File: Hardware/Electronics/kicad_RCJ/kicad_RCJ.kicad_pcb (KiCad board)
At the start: 2 copper layers, 71 parts, among them J10 Conn_01x04_M1_extra, J11 Conn_01x04_M2_extra, J12 Conn_01x04_M3_extra, J13 Conn_01x04_M4_extra, J14 Conn_01x06_teensy_left_extra, J15 Conn_01x04_teensy_right_extra, J16 Conn_01x07_IO_expander_extra, J17 Conn_02x03_I2C, J18 Conn_02x05_3V3_GND, J19 Conn_02x05_5V_GND, J2 Conn_01x06_IMU_extra, J20 Conn_01x06_BNO085_extra, J21 Conn_01x06_ISM20948_extra, J22 Conn_01x02_LSM5DSOX_LIS3MDL_e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, J3 Conn_01x02_colsens_interrupt, J4 Conn_01x02_5V, J5 Conn_01x02_3V3, J6 Conn_01x02_I2C1, J7 Conn_01x01_LOP, J8 Conn_01x03_IO_expander_interr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, J9 Conn_01x06_LED, M5 Servo1, M6 Servo2, U1 DRV8874, U12 VL53L0/1X, U13 VL53L0/1X, U14 VL53L0/1X, U15 VL53L0/1X, U16 VL53L0/1X, U17 VL53L0/1X, U18 VL53L0/1X, U2 DRV8874, U20 BNO085, U21 ICM20948, U22 LSM6DSOX+LIS3MDL, U23 TCS34725, U24 APDS9960, U25 VL53L0/1X, U3 DRV8874, U4 DRV8874

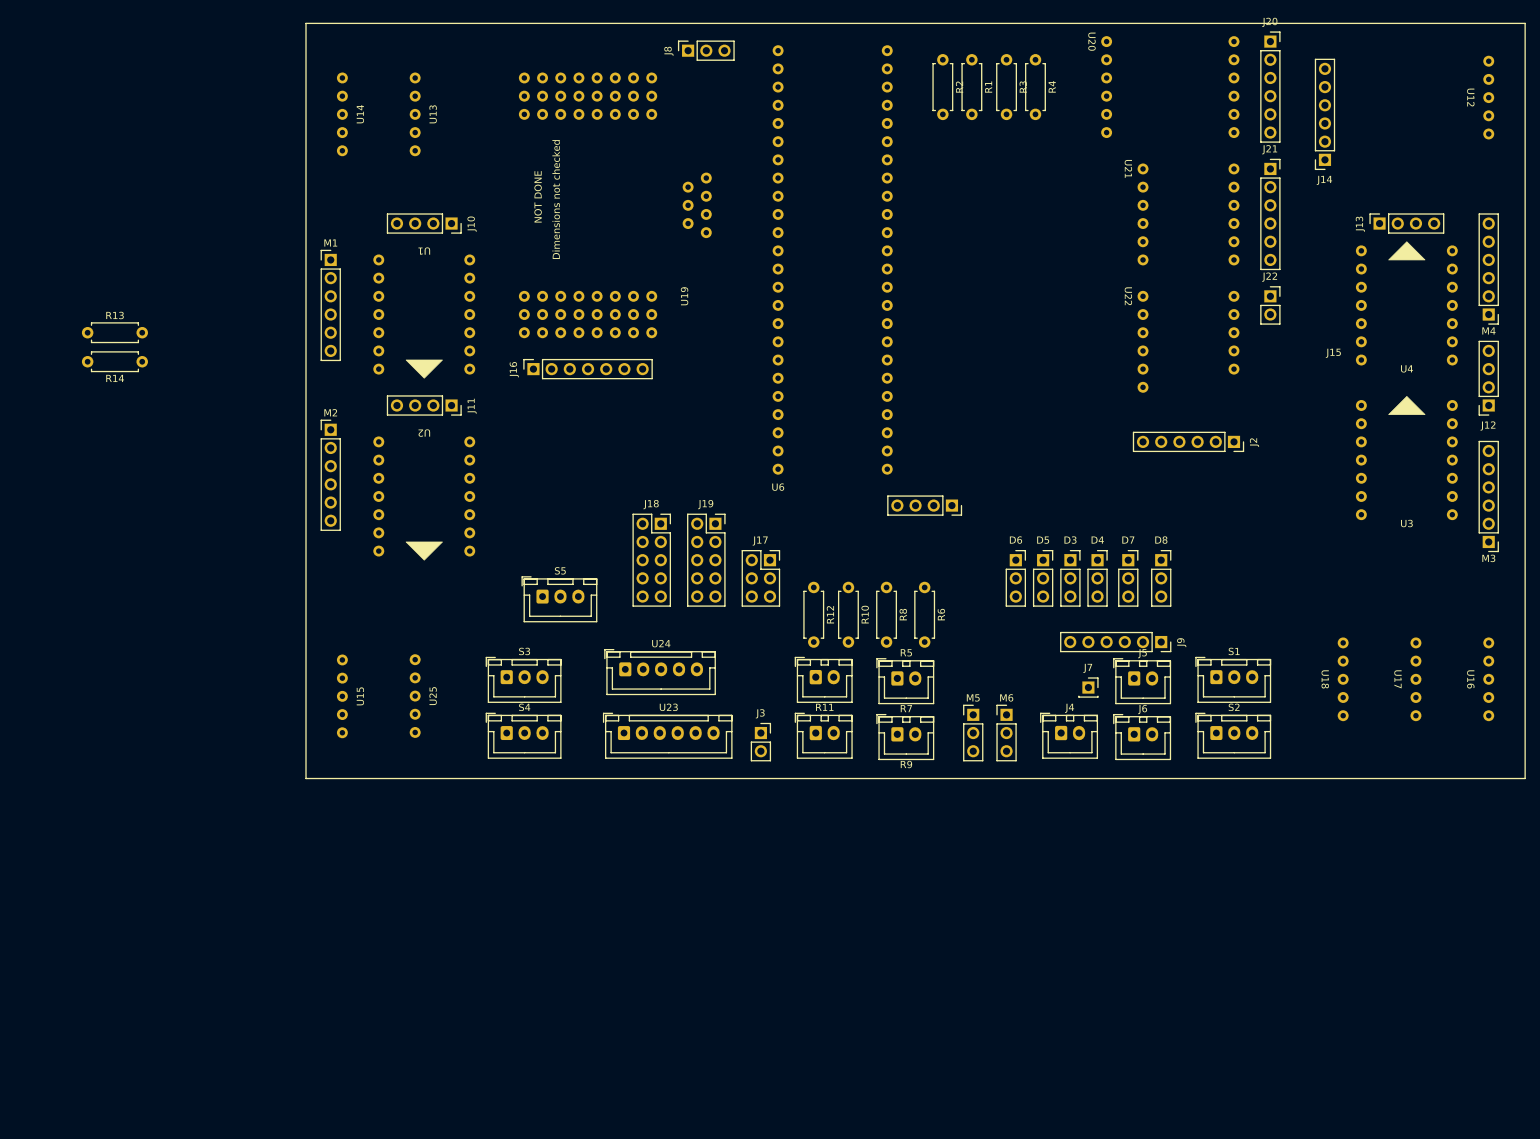
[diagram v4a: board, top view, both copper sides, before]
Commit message: added size constraints to PCB outline and changed layout accordingly
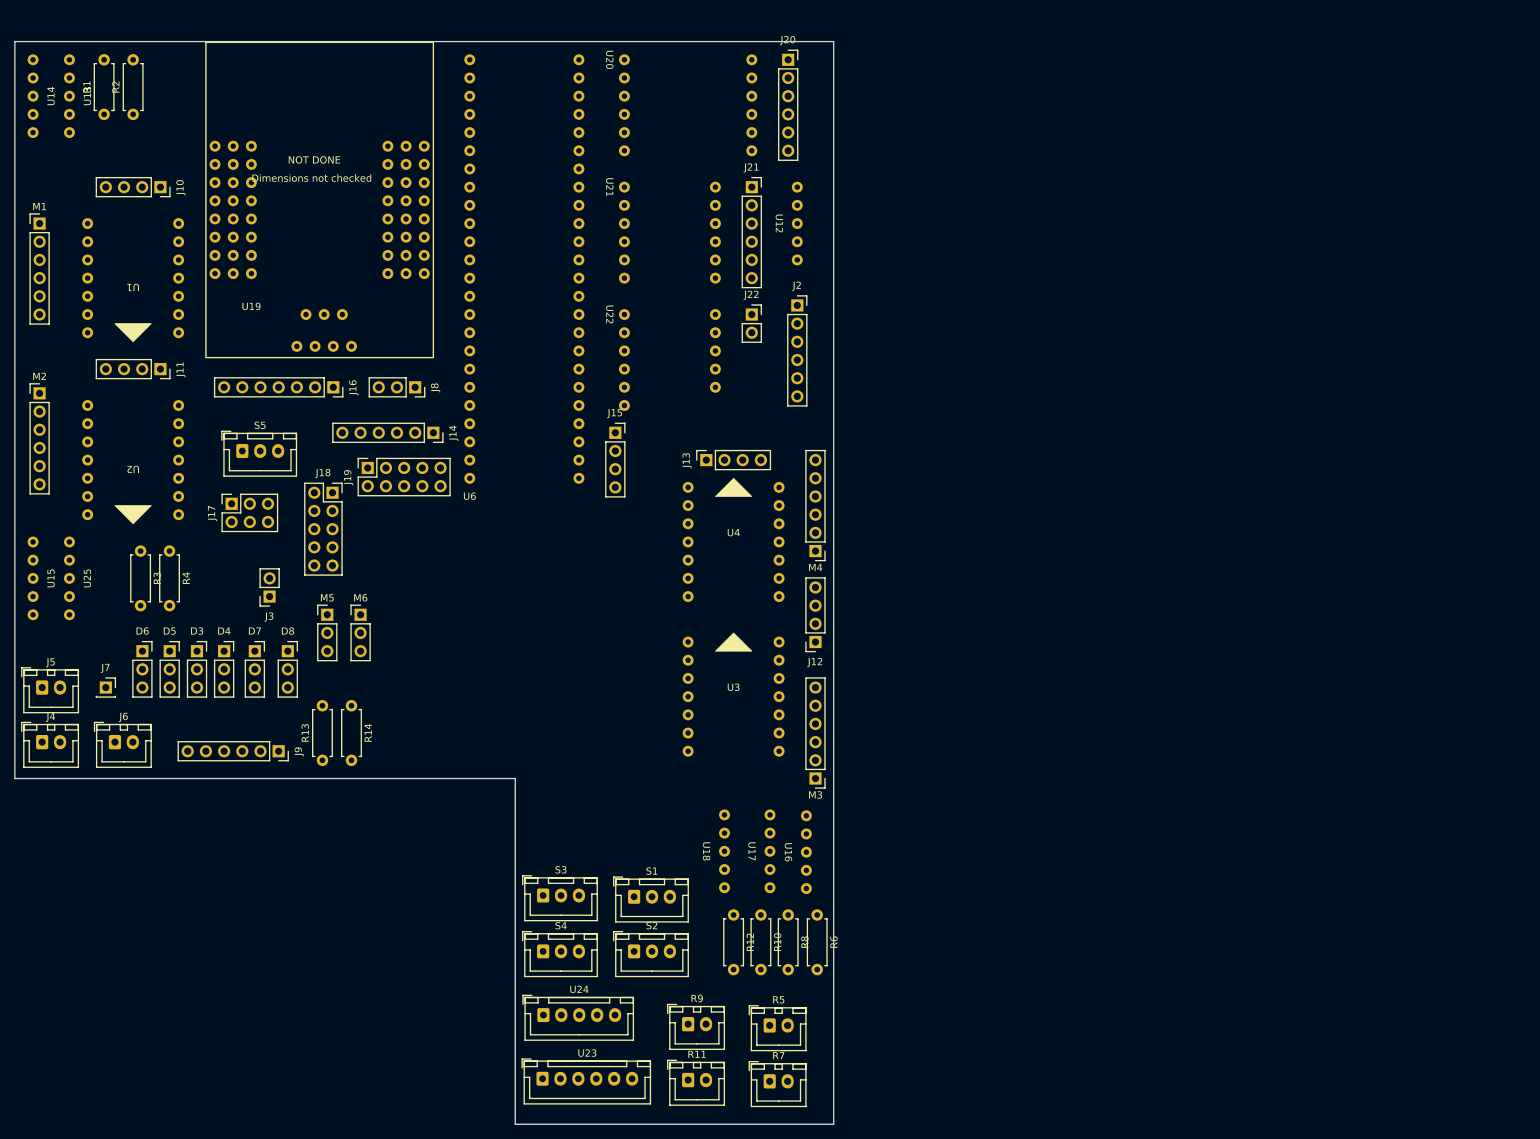
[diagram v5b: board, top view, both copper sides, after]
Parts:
- moved J5 152.4 mm to (36.8, 123.2)
- moved J6 142.3 mm to (47.0, 130.8)
- moved J4 142.2 mm to (36.8, 130.8)
- moved R3 139.0 mm to (50.6, 104.1)
- moved R4 139.0 mm to (54.6, 104.1)
- moved J7 137.2 mm to (45.7, 123.2)
- moved J14 130.2 mm to (91.4, 87.6), turned to -90 degrees
- moved J9 124.1 mm to (69.8, 132.1)
- moved D3 122.6 mm to (58.4, 118.1)
- moved D4 122.6 mm to (62.2, 118.1)
- moved D5 122.6 mm to (54.6, 118.1)
- moved D6 122.6 mm to (50.8, 118.1)
- moved D7 122.6 mm to (66.5, 118.1)
- moved D8 122.6 mm to (71.1, 118.1)
- moved R1 121.4 mm to (45.5, 43.2), turned to 90 degrees
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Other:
- board outline added: 114.3 x 151.1 mm

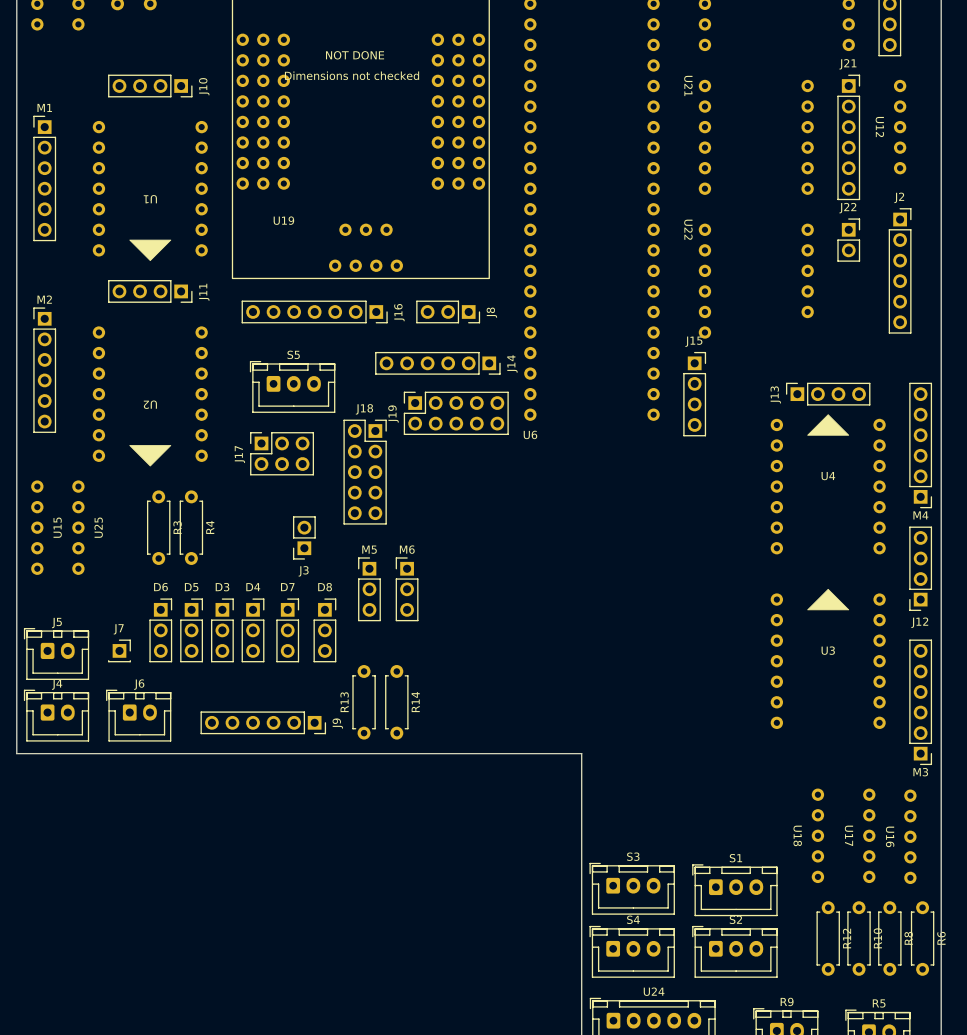
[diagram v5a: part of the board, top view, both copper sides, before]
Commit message: added power delivery to PCB
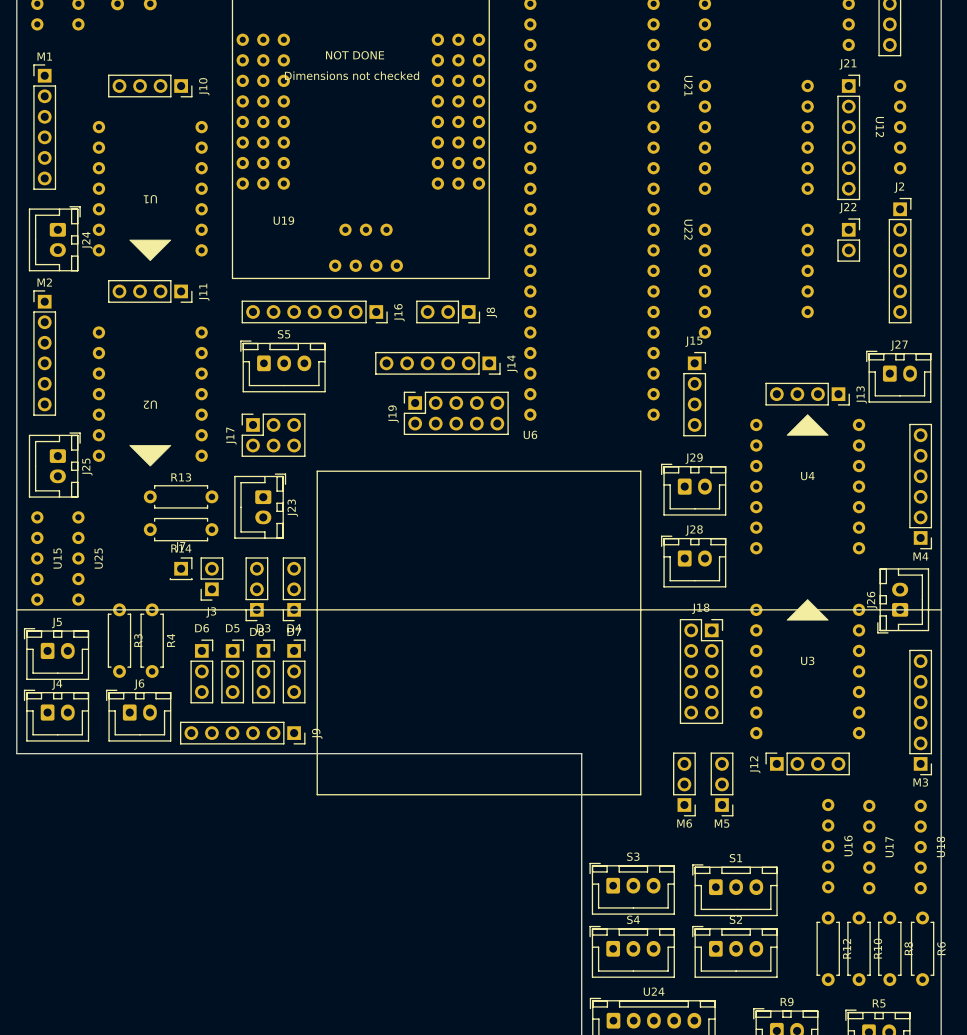
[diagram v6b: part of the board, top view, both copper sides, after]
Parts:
- added J23: VBAT_meas_conn, Connector_JST:JST_XH_B2B-XH-A_1x02_P2.50mm_Vertical, F.Cu at (63.5, 104.2)
- added J24: Conn_01x02, Connector_JST:JST_XH_B2B-XH-A_1x02_P2.50mm_Vertical, F.Cu at (38.1, 71.1)
- added J25: Conn_01x02, Connector_JST:JST_XH_B2B-XH-A_1x02_P2.50mm_Vertical, F.Cu at (38.1, 99.1)
- added J26: Conn_01x02, Connector_JST:JST_XH_B2B-XH-A_1x02_P2.50mm_Vertical, F.Cu at (142.2, 118.1)
- added J27: Conn_01x02, Connector_JST:JST_XH_B2B-XH-A_1x02_P2.50mm_Vertical, F.Cu at (141.0, 88.9)
- added J28: Conn_01x02_5V, Connector_JST:JST_XH_B2B-XH-A_1x02_P2.50mm_Vertical, F.Cu at (115.6, 111.8)
- added J29: Conn_01x02_3.3V, Connector_JST:JST_XH_B2B-XH-A_1x02_P2.50mm_Vertical, F.Cu at (115.6, 102.9)
- moved M5 52.5 mm to (120.2, 142.2), turned to 180 degrees
- moved J18 48.3 mm to (119.0, 120.7)
- moved M6 45.0 mm to (115.6, 142.2), turned to 180 degrees
- moved R13 39.4 mm to (49.5, 104.1), turned to 0 degrees
- moved R14 28.8 mm to (57.1, 108.2), turned to 180 degrees
- moved J12 27.0 mm to (127.0, 137.2), turned to 90 degrees
- moved U18 17.2 mm to (144.8, 152.5), turned to 90 degrees
- moved U16 15.2 mm to (133.3, 152.4), turned to 90 degrees
- moved R3 14.8 mm to (45.7, 118.1)
- moved R4 14.8 mm to (49.8, 118.1)
- moved J7 12.7 mm to (53.3, 113.0)
- moved J3 12.5 mm to (57.1, 115.6)
- moved U17 11.6 mm to (138.4, 152.5), turned to 90 degrees
- moved D8 8.41 mm to (62.7, 118.1), turned to 180 degrees
- moved D4 7.18 mm to (67.3, 123.2)
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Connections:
- J9 pad 1: Net-(D8-SIGNAL) -> Net-(D4-SIGNAL)
- J9 pad 2: Net-(D7-SIGNAL) -> Net-(D3-SIGNAL)
- J9 pad 3: Net-(D4-SIGNAL) -> Net-(D5-SIGNAL)
- J9 pad 4: Net-(D3-SIGNAL) -> Net-(D6-SIGNAL)
- J9 pad 5: Net-(D5-SIGNAL) -> Net-(D7-SIGNAL)
- J9 pad 6: Net-(D6-SIGNAL) -> Net-(D8-SIGNAL)

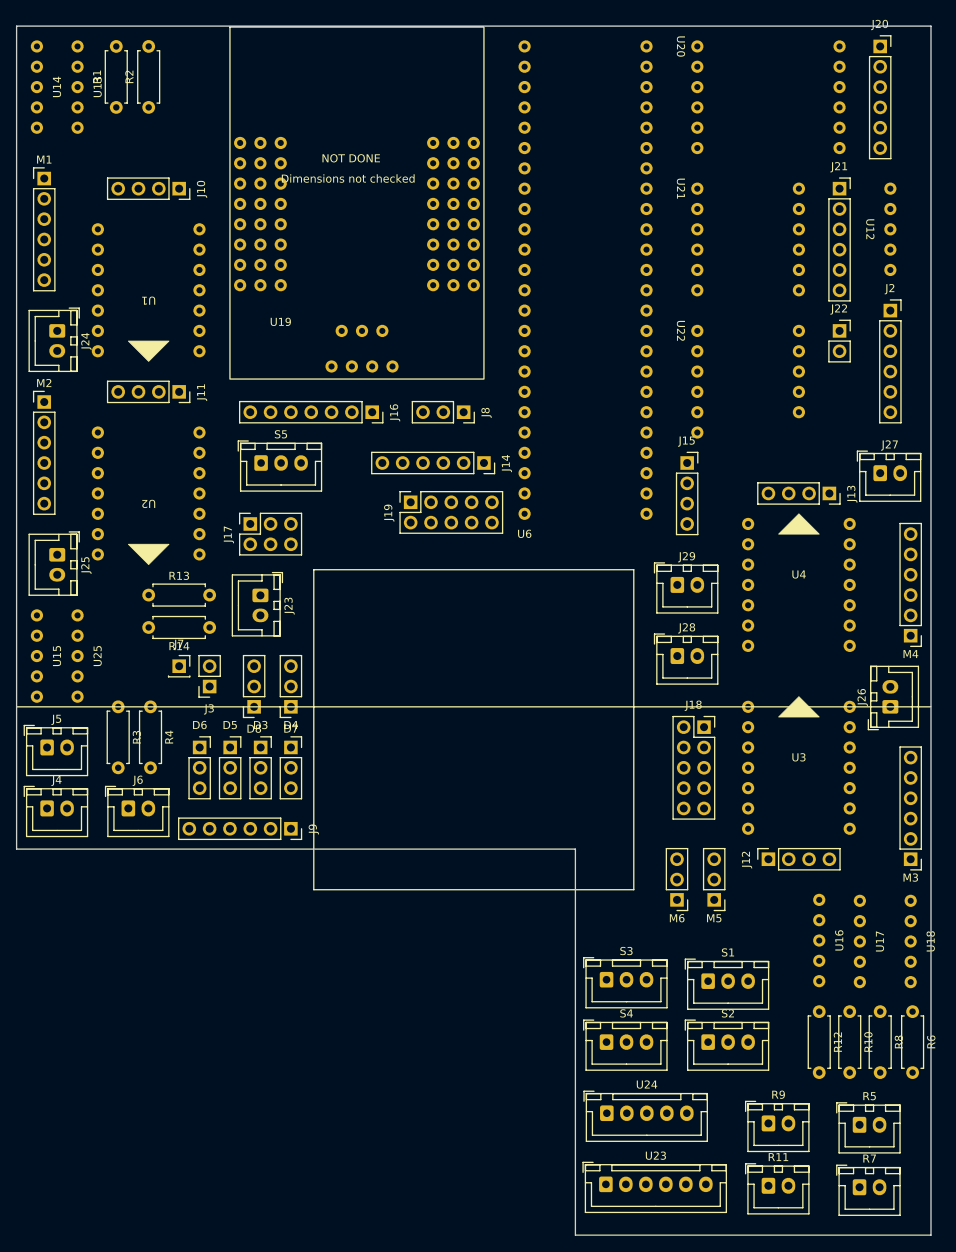
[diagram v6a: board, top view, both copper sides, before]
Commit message: added courtyards to most custom footprints
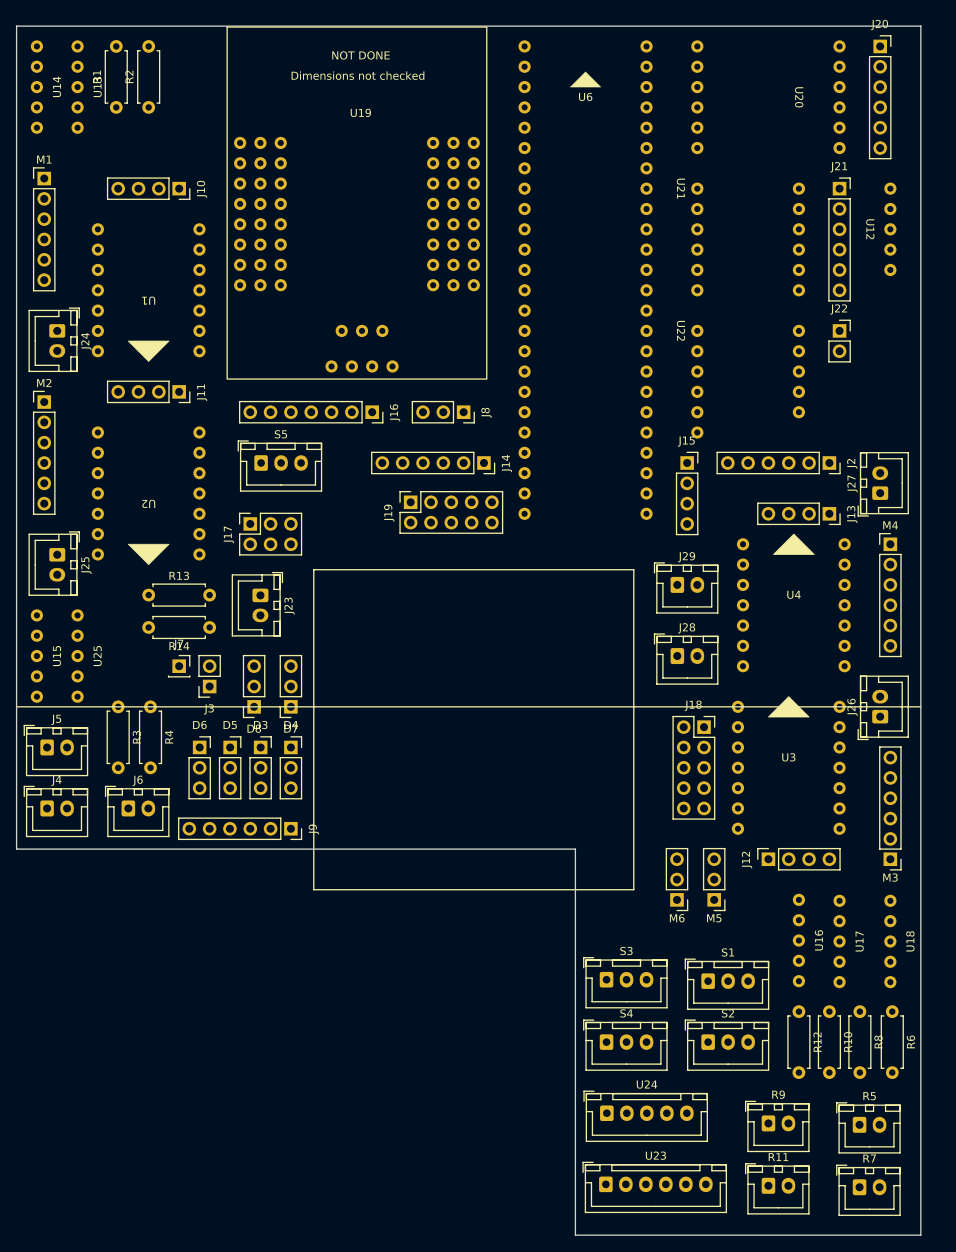
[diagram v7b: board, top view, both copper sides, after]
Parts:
- moved J2 20.5 mm to (134.6, 87.6), turned to -90 degrees
- moved M4 11.7 mm to (142.2, 97.8), turned to 0 degrees
- moved U4 2.62 mm to (123.8, 113.0)
- moved R6 2.54 mm to (142.5, 156.2)
- moved U17 2.54 mm to (135.9, 152.5)
- moved J13 2.54 mm to (134.6, 94.0)
- moved M3 2.54 mm to (142.2, 137.2)
- moved R10 2.54 mm to (134.6, 156.2)
- moved R12 2.54 mm to (130.8, 156.2)
- moved R8 2.54 mm to (138.4, 156.2)
- moved U16 2.54 mm to (130.8, 152.4)
- moved U18 2.54 mm to (142.2, 152.5)
- moved J27 2.50 mm to (141.0, 91.4), turned to 90 degrees
- moved J26 1.77 mm to (141.0, 119.3)
- moved U3 1.27 mm to (123.2, 133.3)
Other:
- board size 114.3 x 151.1 mm -> 113 x 151.1 mm

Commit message: fixed some connector pin number issues (TOF and colour sensors)
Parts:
- U12, U13, U14, U15, U16, U17, U18, U25: footprint RCJ2024_kicad_footprints:VL53L0X_VL53L1X_connector -> Connector_JST:JST_XH_B5B-XH-A_1x05_P2.50mm_Vertical
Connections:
- U12 pad 2: +3.3V -> GND
- U12 pad 3: GND -> SDA
- U12 pad 4: SDA -> SCL
- U12 pad 5: SCL -> Net-(U12-SCL)
- U13 pad 2: +3.3V -> GND
- U13 pad 3: GND -> SDA
- U13 pad 4: SDA -> SCL
- U13 pad 5: SCL -> Net-(U13-SCL)
- U14 pad 2: +3.3V -> GND
- U14 pad 3: GND -> SDA
- U14 pad 4: SDA -> SCL
- U14 pad 5: SCL -> Net-(U14-SCL)
- U15 pad 2: +3.3V -> GND
- U15 pad 3: GND -> SDA
- U15 pad 4: SDA -> SCL
- U15 pad 5: SCL -> Net-(U15-SCL)
- U16 pad 2: +3.3V -> GND
- U16 pad 3: GND -> SDA
- U16 pad 4: SDA -> SCL
- U16 pad 5: SCL -> Net-(U16-SCL)
- U17 pad 2: +3.3V -> GND
- U17 pad 3: GND -> SDA
- U17 pad 4: SDA -> SCL
- U17 pad 5: SCL -> Net-(U17-SCL)
- U18 pad 2: +3.3V -> GND
- U18 pad 3: GND -> SDA
- U18 pad 4: SDA -> SCL
- U18 pad 5: SCL -> Net-(U18-SCL)
- U19 pad 10: Net-(U15-XSHUT) -> Net-(U15-SCL)
- U19 pad 11: Net-(U13-XSHUT) -> Net-(U13-SCL)
- U19 pad 12: Net-(U16-XSHUT) -> Net-(U16-SCL)
- U19 pad 13: Net-(U14-XSHUT) -> Net-(U14-SCL)
- U19 pad 14: Net-(U17-XSHUT) -> Net-(U17-SCL)
- U19 pad 15: Net-(U18-XSHUT) -> Net-(U18-SCL)
- U19 pad 9: Net-(U12-XSHUT) -> Net-(U12-SCL)
- U23 pad 5: unconnected-(U23-3V3-Pad5) -> GND
- U23 pad 6: GND -> +3.3V
- U24 pad 2: unconnected-(U24-3Vo-Pad2) -> GND
- U24 pad 3: GND -> SCL
- U24 pad 4: SCL -> SDA
- U24 pad 5: SDA -> Net-(J3-Pin_1)
- U25 pad 2: +3.3V -> GND
- U25 pad 3: GND -> SDA
- U25 pad 4: SDA -> SCL
- U25 pad 5: SCL -> Net-(U19-PB7)
